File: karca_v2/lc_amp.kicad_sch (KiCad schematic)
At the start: 20 parts, among them U18 AD8223, U6 TLV9304xD, U7 TLV9304xD

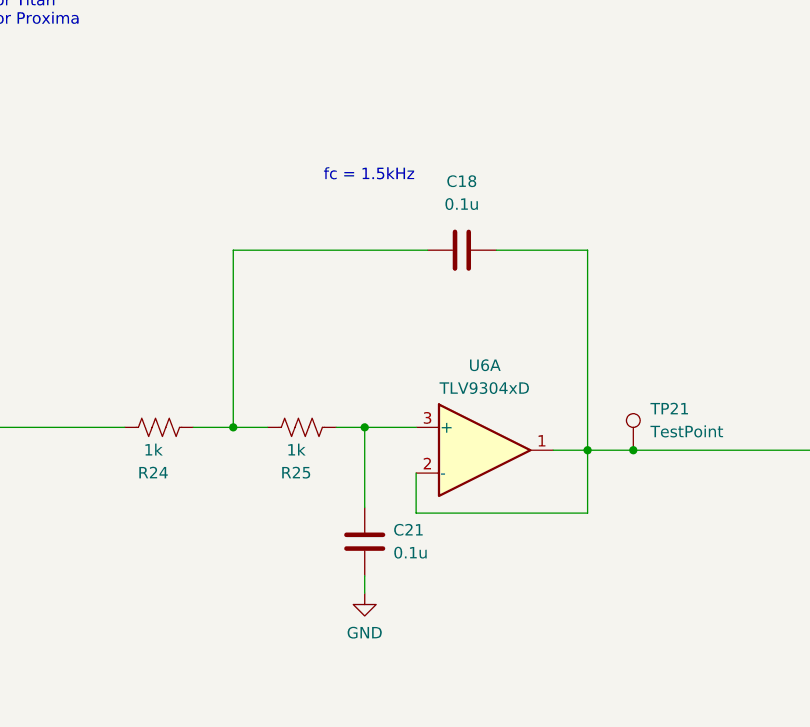
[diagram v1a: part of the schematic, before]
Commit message: finished schematic for v2.1
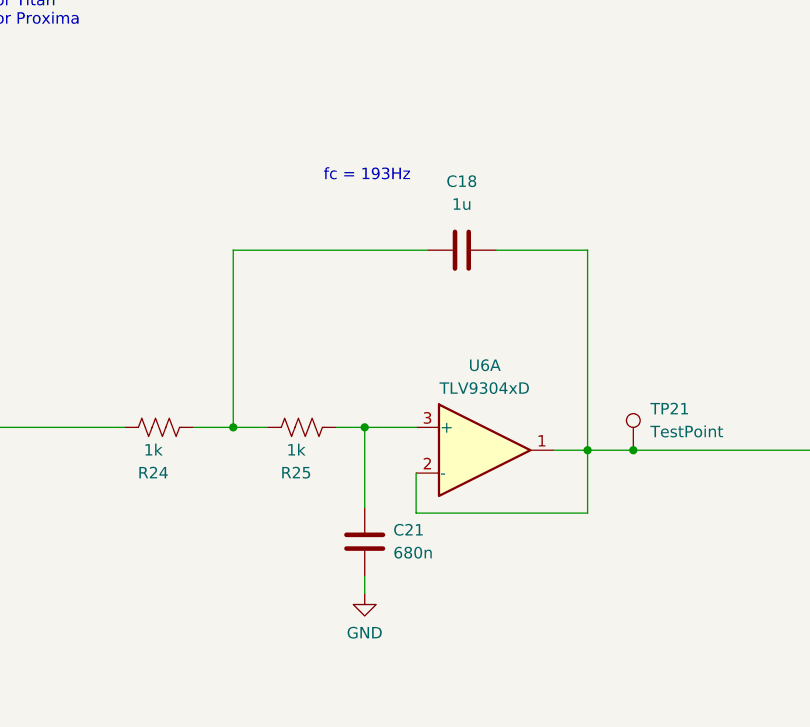
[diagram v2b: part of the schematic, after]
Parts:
- C18: value 0.1u -> 1u
- C21: value 0.1u -> 680n
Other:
- note added: "fc = 193Hz"
- note removed: "fc = 1.5kHz"
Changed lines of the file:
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@@
 		)
 	)
-	(text "fc = 1.5kHz\n"
+	(text "fc = 193Hz\n"
 		(exclude_from_sim no)
 		(at 175.768 47.752 0)
@@
 			)
 		)
-		(property "Value" "0.1u"
+		(property "Value" "1u"
 			(at 191.135 50.165 90)
 			(effects
@@
 			)
 		)
-		(property "Value" "0.1u"
+		(property "Value" "680n"
 			(at 183.515 88.9 0)
 			(effects

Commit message: swapped adcs
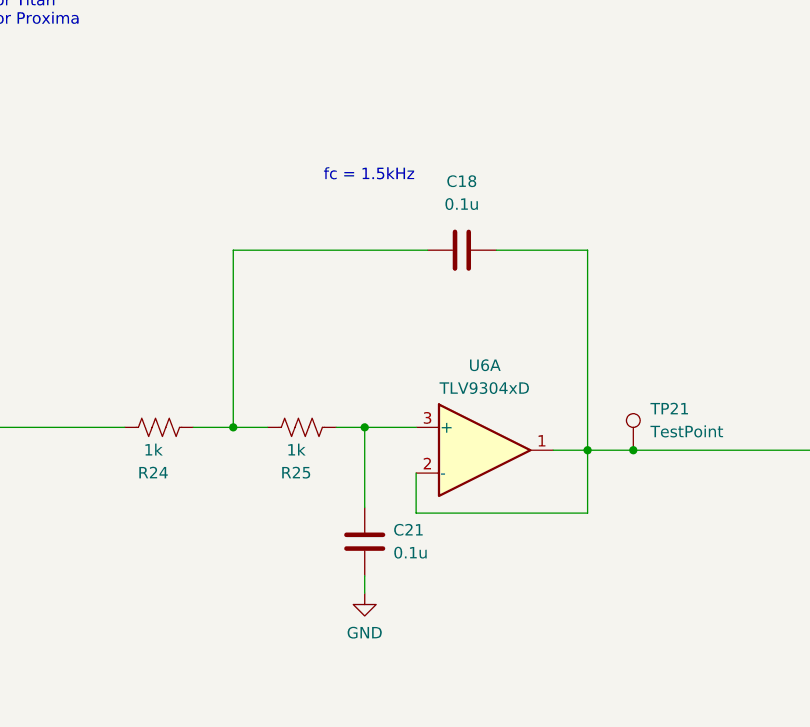
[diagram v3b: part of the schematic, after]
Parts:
- C18: value 1u -> 0.1u
- C21: value 680n -> 0.1u
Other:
- note added: "fc = 1.5kHz"
- note removed: "fc = 193Hz"
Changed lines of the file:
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@@
 	(title_block
 		(title "kARCA 2.0 Engine Control System")
-		(date "2026-03-23")
-		(rev "1.2")
+		(date "2024-12-16")
+		(rev "1.1")
 		(company "Rice Eclipse")
 		(comment 1 "Designed by Deepak Narayan")
@@
 		)
 	)
-	(text "fc = 193Hz\n"
+	(text "fc = 1.5kHz\n"
 		(exclude_from_sim no)
 		(at 175.768 47.752 0)
@@
 			)
 		)
-		(property "Value" "1u"
+		(property "Value" "0.1u"
 			(at 191.135 50.165 90)
 			(effects
@@
 			)
 		)
-		(property "Value" "680n"
+		(property "Value" "0.1u"
 			(at 183.515 88.9 0)
 			(effects
